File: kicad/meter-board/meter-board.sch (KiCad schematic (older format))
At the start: 55 parts, among them P1 CONN_2, P10 CONN_3, P11 CONN_3, P2 CONN_5, P3 CONN_3, P4 CONN_3, P5 CONN_3, P6 CONN_3, P7 CONN_3, P8 CONN_3, P9 CONN_3, SW1 SW_PUSH_SMALL, U1 PANSTAMP_02, U2 UA78M33

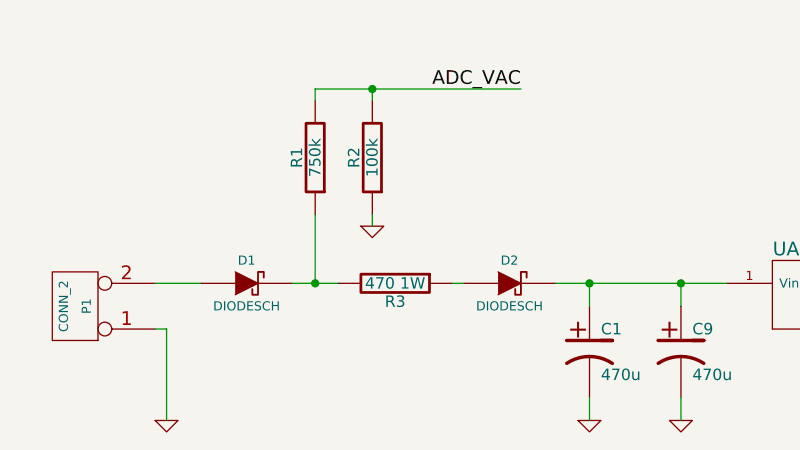
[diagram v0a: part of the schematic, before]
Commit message: Limiting resistor changed to 47 ohm
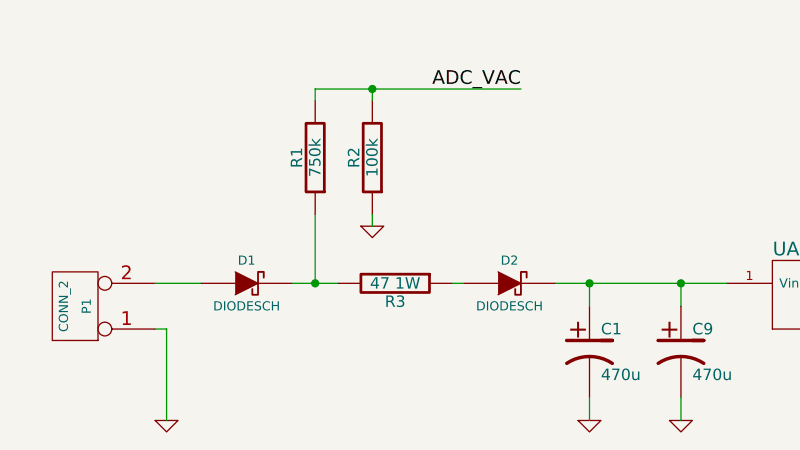
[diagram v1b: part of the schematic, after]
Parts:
- R3: value 470 1W -> 47 1W
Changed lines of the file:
@@
-EESchema Schematic File Version 2  date Tue 12 Jun 2012 04:27:57 PM CEST
+EESchema Schematic File Version 2  date Tue 11 Sep 2012 12:17:21 PM CEST
 LIBS:power
 LIBS:device
@@
 LIBS:microchip-mcp125x-xxx
 LIBS:toshiba
-LIBS:meter-cache
+LIBS:meter-board-cache
 EELAYER 24  0
 EELAYER END
@@
 Sheet 1 1
 Title "panStamp Energy Meter board"
-Date "12 jun 2012"
+Date "11 sep 2012"
 Rev "01"
-Comp "uSapiens (www.usapiens.com)"
+Comp "panStamp"
 Comment1 ""
 Comment2 ""
@@
 P 2450 6850
 F 0 "R3" V 2530 6850 50  0000 C CNN
-F 1 "470 1W" V 2450 6850 50  0000 C CNN
+F 1 "47 1W" V 2450 6850 50  0000 C CNN
 F 2 "SM2512" H 2450 6850 60  0001 C CNN
 	1    2450 6850

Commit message: Version 0.2 committed
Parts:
- removed C9: 470u, SMDCPOL_12, symbol CP1
- removed D1: DIODESCH, SMA, symbol DIODESCH
- added C14: 100n, SM0603S, symbol C
- added P12, P13: CONN_3, audio_jack_smd_01, symbol CONN_3
- added R26, R27: 2k, SM0603S, symbol R
- added R28, R29: 10k, SM0603S, symbol R
- added R30, R31: 470k, SM0603S, symbol R
- added R32: 100, SM0603S, symbol R
- added U3: H11AA1, symbol OPTO-TRANSISTOR
- renumbered D2 to D1
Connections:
- net +3.3V: now also P12.3 (P3), R28.1, R30.2
- net ADC_CT1: now also P4.3 (P3), R12.2; no longer P3.3 (P3), R11.2
- net ADC_CT2: now also P5.3 (P3), R13.2; no longer P4.3 (P3), R12.2
- net ADC_CT3: now also P6.3 (P3), R24.2; no longer P5.3 (P3), R13.2
- net ADC_CT4: now also P7.3 (P3), R23.2; no longer P6.3 (P3), R24.2
- net ADC_CT5: now also P8.3 (P3), R25.2; no longer P7.3 (P3), R23.2
- net ADC_CT6: now also P13.3 (P3), R32.2; no longer P8.3 (P3), R25.2
- net ADC_VAC: now also R26.2
- net COUNTER1: now also P10.2 (PM), R15.2, U1.21 (D6); no longer P9.2 (PM), R14.2, U1.20 (D5)
- net COUNTER2: now also P11.2 (PM), R16.2, U1.22 (D7); no longer P10.2 (PM), R15.2, U1.21 (D6)
- net COUNTER3: now also U1.2 (D8), P12.2 (PM), R29.2; no longer P11.2 (PM), R16.2, U1.22 (D7)
- net GND: now also C14.2, P12.1 (P1), R27.2, R29.1, R31.1, U3.4 (E)
- net ADC_CT0: now reaches U1.12 (A7)
- net ADC_CT0: now also P3.3 (P3), R11.2
- net ZEROC_INT: now reaches U1.18 (D3(INT1))
- net ZEROC_INT: now also R28.2, U3.5 (C)
- net at P1.2 (PM): now also R1.1, R3.2
- new net: R26.1, U3.1 (A)
- new net: R27.1, U3.2 (K)
- new net: C14.1, P13.1 (P1), R30.1, R31.2, R32.1
- new net COUNTER0: P9.2 (PM), R14.2, U1.20 (D5)
- no-connect marks 15 -> 14
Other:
- moved on the sheet: C10, C11, C12, C5, C6, C7, P1, P3, P4, P5, P6, P7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

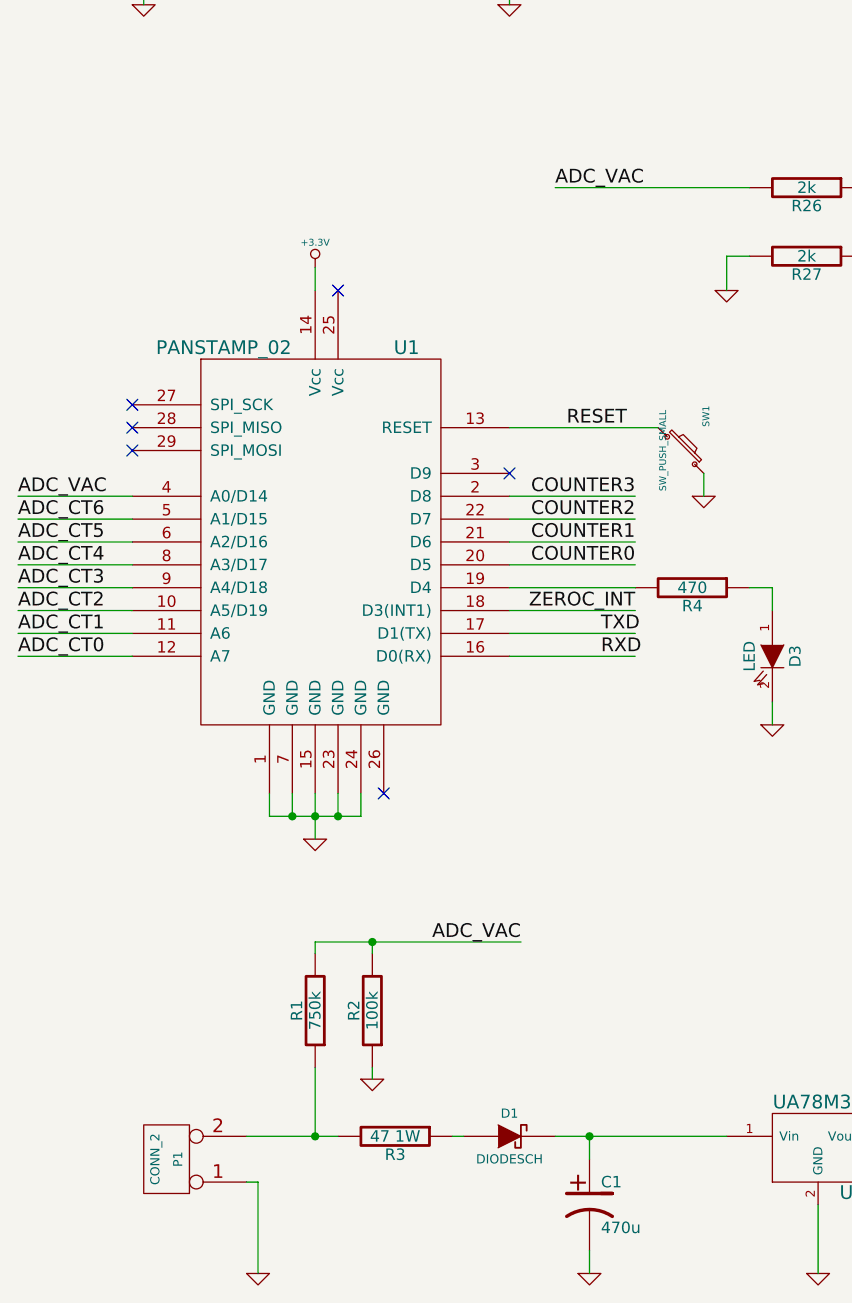
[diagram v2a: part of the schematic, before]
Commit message: zero-crossing detector connected to the original AC signal
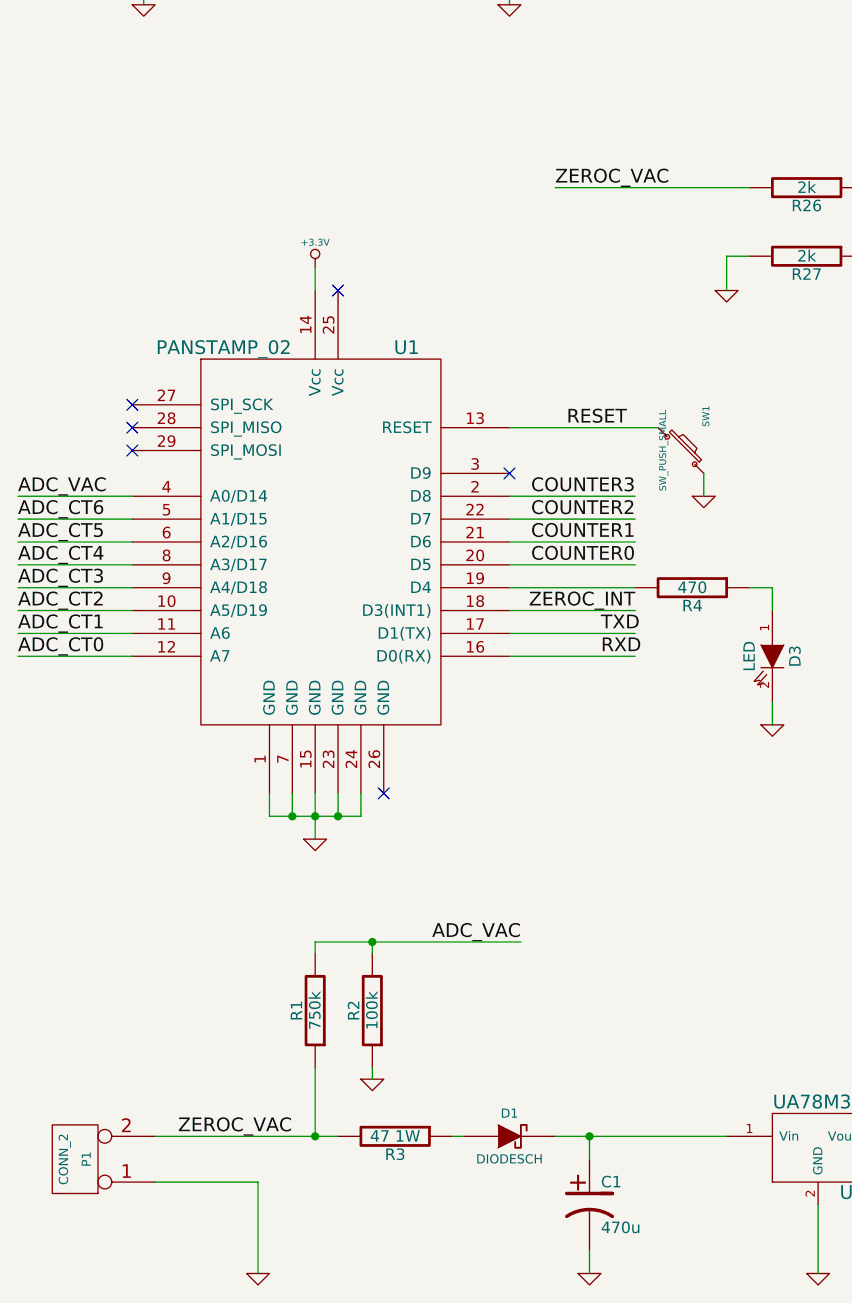
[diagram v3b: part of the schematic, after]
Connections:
- net ADC_VAC: no longer R26.2
- net ZEROC_VAC: now reaches P1.2 (PM), R1.1, R3.2
- net ZEROC_VAC: now also R26.2
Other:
- moved on the sheet: P1
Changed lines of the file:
@@
-EESchema Schematic File Version 2  date Thu 01 Nov 2012 06:59:10 PM CET
+EESchema Schematic File Version 2  date Wed 07 Nov 2012 06:59:29 PM CET
 LIBS:power
 LIBS:device
@@
 Sheet 1 1
 Title "panStamp Energy Meter board"
-Date "1 nov 2012"
+Date "7 nov 2012"
 Rev "02"
 Comp "panStamp"
@@
 Comment4 ""
 $EndDescr
-Text Label 3500 4350 2    60   ~ 0
-COUNTER0
+Text Label 1500 6850 0    60   ~ 0
+ZEROC_VAC
+Wire Wire Line
+	1400 7050 1850 7050
 Wire Wire Line
 	2950 4050 3500 4050
-Text Label 800  4750 0    60   ~ 0
-ADC_CT0
 Wire Wire Line
 	1300 4750 800  4750
@@
 	2100 6550 2100 6850
 Wire Wire Line
-	1800 6850 2200 6850
-Wire Wire Line
 	7850 5600 8550 5600
 Wire Wire Line
@@
 	2350 6000 2350 6050
 Wire Wire Line
-	1850 7450 1850 7050
-Wire Wire Line
-	1850 7050 1800 7050
+	1850 7050 1850 7450
 Wire Wire Line
 	7600 3500 7600 3550
@@
 Wire Wire Line
 	6350 1800 6350 1900
+Wire Wire Line
+	1400 6850 2200 6850
+Text Label 3500 4350 2    60   ~ 0
+COUNTER0
+Text Label 800  4750 0    60   ~ 0
+ADC_CT0
 $Comp
 L CONN_3 P12
@@
 $EndComp
 Text Label 3150 2700 0    60   ~ 0
-ADC_VAC
+ZEROC_VAC
 Text Label 6700 2800 2    60   ~ 0
 ZEROC_INT
@@
 L CONN_2 P1
 U 1 1 4E2D91DA
-P 1450 6950
-F 0 "P1" V 1400 6950 40  0000 C CNN
-F 1 "CONN_2" V 1500 6950 40  0000 C CNN
-F 2 "terminal_0.2_right_2" H 1450 6950 60  0001 C CNN
-	1    1450 6950
-	-1   0    0    1
-$EndComp
+P 1050 6950
+F 0 "P1" V 1000 6950 40  0000 C CNN
+F 1 "CONN_2" V 1100 6950 40  0000 C CNN
+F 2 "terminal_0.2_right_2" H 1050 6950 60  0001 C CNN
+	1    1050 6950
+	-1   0    0    1
+$EndComp
